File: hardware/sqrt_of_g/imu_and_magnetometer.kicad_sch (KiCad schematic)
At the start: 9 parts, among them U6 RM3100 Dev Board, U7 BMI270

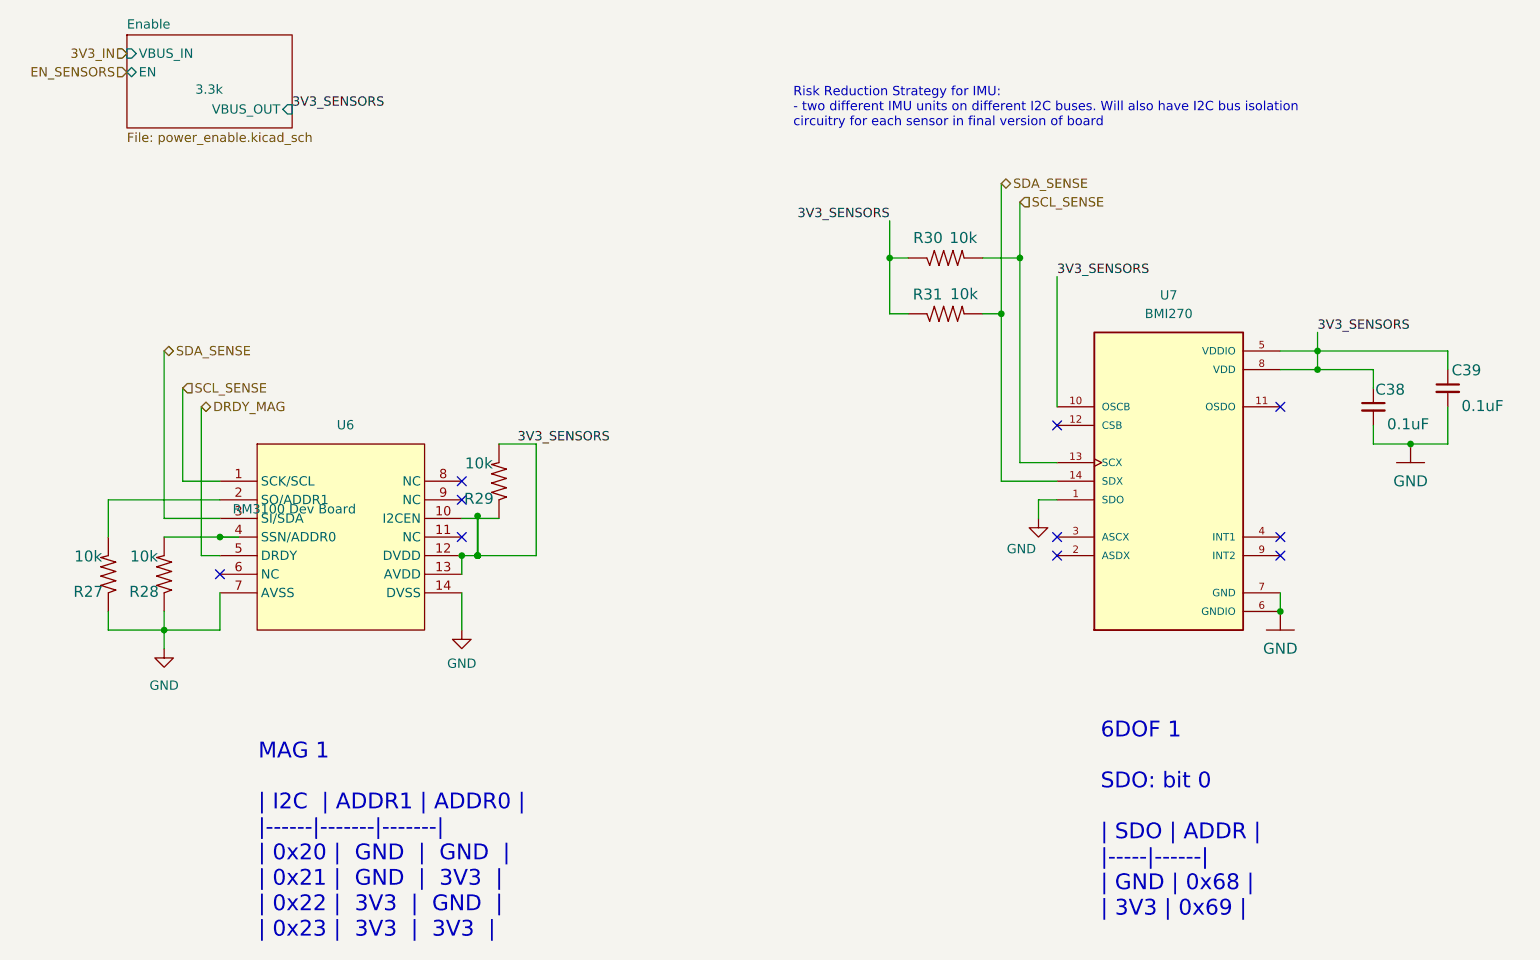
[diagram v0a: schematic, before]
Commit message: fix landing pattern
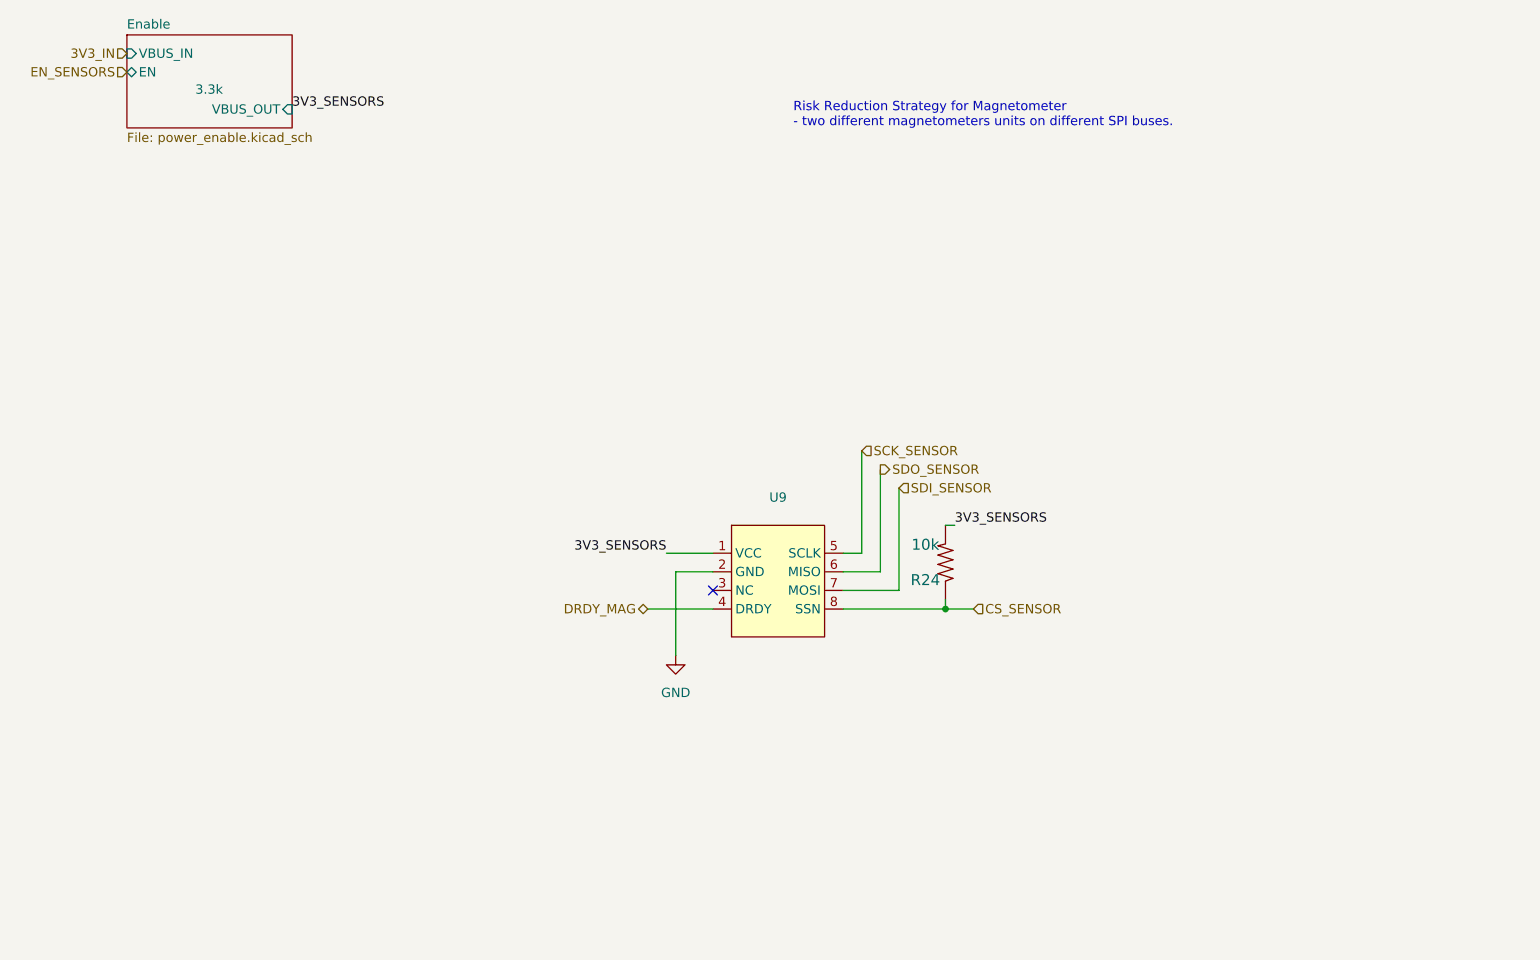
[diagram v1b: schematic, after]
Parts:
- removed C38, C39: 0.1uF, Capacitor_SMD:C_0603_1608Metric, symbol mainboard:C_Small
- removed R27, R28, R30, R31: 10k, Resistor_SMD:R_0603_1608Metric, symbol mainboard:R-US_R0603
- removed U6: RM3100 Dev Board, adcs:RM3100, symbol adcs:RM3100
- removed U7: BMI270, adcs:XDCR_BMI270, symbol mainboard:BMI270
- added U9: ~, adcs:RM3100CB, symbol adcs:RM3100-CB_AliExpress
- R24: renamed from R29; footprint Resistor_SMD:R_0603_1608Metric -> Resistor_SMD:R_0402_1005Metric
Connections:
- net 3V3_SENSORS: now also U9.1 (VCC)
- net DRDY_MAG: now also U9.4 (DRDY)
- net GND: now also U9.2 (GND)
- net CS_SENSOR: now reaches R24.1
- net CS_SENSOR: now also U9.8 (SSN)
- new net SCK_SENSOR: U9.5 (SCLK)
- new net SDI_SENSOR: U9.7 (MOSI)
- new net SDO_SENSOR: U9.6 (MISO)
- no-connect marks 10 -> 1
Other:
- note added: "Risk Reduction Strategy for Magnetometer - two different magnetometers units on different SPI buses."
- note removed: "6DOF 1 SDO: bit 0 | SDO | ADDR | |-----|------| | GND | 0x68 | | 3V3 | 0x69 |"
- note removed: "MAG 1 | I2C | ADDR1 | ADDR0 | |------|-------|-------| | 0x20 | GND | GND | | 0x21 | GND | 3V3 | | 0x22 | 3V3 | GND | | 0x23 | 3V3 | 3V3 |"
- note removed: "Risk Reduction Strategy for IMU: - two different IMU units on different I2C buses. Will also have I2C bus isolation circuitry for each sensor in final version of board"
- title: (none) -> √g
- moved on the sheet: R24
